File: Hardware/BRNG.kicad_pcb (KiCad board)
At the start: 2 copper layers, 120 x 70 mm, 92 parts, among them J2 MOLEX 105017 0001, J3 CONNETTORE FEMMINA 6 PIN 90°, Q1 BC847, Q2 BC847, Q3 MMBTA42, Q4 BC847, Q5 BC847, SW1 DIPTRONICS NDI-02H-V, U1 LM555N, U2 ATMEGA328-AU, U3 LM555N, U4 CH340G, Y1 16MHz LF XTAL003237, Y2 12MHz LF XTAL003210

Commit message: Fixes #5
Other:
- board text added: "Rev 1 - May 2018 valerionappi.it github.com/5N44P"
- board text removed: "Rev 0 - Mar 2018 valerionappi.it github.com/5N44P"
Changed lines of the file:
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@@
-(kicad_pcb (version 20170123) (host pcbnew "(2017-07-16 revision e797af331)-makepkg")
+(kicad_pcb (version 4) (host pcbnew 4.0.7)
   (general
+    (links 167)
+    (no_connects 1)
+    (area 72.943571 51.449999 211.642858 121.550001)
     (thickness 1.6)
     (drawings 44)
@@
     (visible_elements 7FFFFFFF)
     (pcbplotparams
-      (layerselection 0x010f0_ffffffff)
-      (usegerberextensions false)
+      (layerselection 0x010f0_80000001)
+      (usegerberextensions true)
       (excludeedgelayer true)
       (linewidth 0.100000)
@@
       (hpglpenspeed 20)
       (hpglpendiameter 15)
+      (hpglpenoverlay 2)
       (psnegative false)
       (psa4output false)
@@
       (drillshape 0)
       (scaleselection 1)
-      (outputdirectory illustration/))
+      (outputdirectory /home/valerio/Scrivania/Gerber/))
   )
   (net 0 "")
@@
     (tags "resistor 0805")
     (attr smd)
-    (fp_text reference R4 (at 3.073094 0.118122) (layer F.SilkS)
+    (fp_text reference R4 (at 3.073094 0.118122 360) (layer F.SilkS)
       (effects (font (size 1 1) (thickness 0.15)))
     )
@@
       (effects (font (size 1 1) (thickness 0.15)))
     )
-    (fp_text user %R (at 0 0) (layer F.Fab)
+    (fp_text user %R (at 0 0 360) (layer F.Fab)
       (effects (font (size 1 1) (thickness 0.15)))
     )
@@
   (module customfootprints:0802_side_led (layer F.Cu)
     (at 94.5 105.75 315)
-    (fp_text reference D9 (at 3.535534 -1.414214) (layer F.SilkS)
+    (fp_text reference D9 (at 3.535534 -1.414214 360) (layer F.SilkS)
       (effects (font (size 1 1) (thickness 0.15)))
     )
@@
   (module customfootprints:0802_side_led (layer F.Cu)
     (at 194.952082 65.202082 135)
-    (fp_text reference D10 (at -2.896193 1.767767) (layer F.SilkS)
+    (fp_text reference D10 (at -2.896193 1.767767 360) (layer F.SilkS)
       (effects (font (size 1 1) (thickness 0.15)))
     )
@@
     (effects (font (size 2 2) (thickness 0.4)))
   )
-  (gr_text "Rev 0 - Mar 2018\nvalerionappi.it\ngithub.com/5N44P" (at 138.75 110) (layer F.SilkS)
+  (gr_text "Rev 1 - May 2018\nvalerionappi.it\ngithub.com/5N44P" (at 138.75 110) (layer F.SilkS)
     (effects (font (size 1 1) (thickness 0.2)) (justify left))
   )
@@
     (effects (font (size 1.5 1.5) (thickness 0.3)))
   )
-  (gr_text RX (at 119 103.5) (layer F.SilkS)
+  (gr_text RX (at 118.872 100.33) (layer F.SilkS)
     (effects (font (size 1.5 1.5) (thickness 0.3)))
   )
-  (gr_text TX (at 119 100.5) (layer F.SilkS)
+  (gr_text TX (at 118.872 103.505) (layer F.SilkS)
     (effects (font (size 1.5 1.5) (thickness 0.3)))
   )
@@
   (segment (start 127.75 67.6) (end 127.75 69.25) (width 0.5) (layer F.Cu) (net 3))
   (via (at 127.75 69.25) (size 0.8) (drill 0.4) (layers F.Cu B.Cu) (net 3))
-  (segment (start 101.7 98.64) (end 100.55 98.64) (width 0.5) (layer F.Cu) (net 4))
-  (segment (start 100.55 98.64) (end 100.16 98.25) (width 0.5) (layer F.Cu) (net 4))
-  (segment (start 101.7 98.64) (end 101.11 98.64) (width 0.5) (layer F.Cu) (net 4))
-  (segment (start 134.295028 79) (end 134 79) (width 0.5) (layer F.Cu) (net 6))
-  (segment (start 134.868122 78.426906) (end 134.295028 79) (width 0.5) (layer F.Cu) (net 6))
-  (segment (start 127.25 79) (end 133.434315 79) (width 0.5) (layer B.Cu) (net 6))
-  (segment (start 125.75 80.5) (end 127.25 79) (width 0.5) (layer B.Cu) (net 6))
-  (segment (start 134.868122 77.176906) (end 134.868122 78.426906) (width 0.5) (layer F.Cu) (net 6))
-  (segment (start 133.434315 79) (end 134 79) (width 0.5) (layer B.Cu) (net 6))
-  (via (at 134 79) (size 0.8) (drill 0.4) (layers F.Cu B.Cu) (net 6))
-  (segment (start 125.5 80.75) (end 125.75 80.5) (width 0.5) (layer F.Cu) (net 6))
-  (segment (start 106.25 80.75) (end 125.5 80.75) (width 0.5) (layer F.Cu) (net 6))
-  (via (at 125.75 80.5) (size 0.8) (drill 0.4) (layers F.Cu B.Cu) (net 6))
-  (segment (start 105.850001 81.149999) (end 106.25 80.75) (width 0.5) (layer B.Cu) (net 6))
-  (segment (start 100.5 86.5) (end 105.850001 81.149999) (width 0.5) (layer B.Cu) (net 6))
-  (segment (start 99 86.5) (end 100.5 86.5) (width 0.5) (layer B.Cu) (net 6))
-  (via (at 106.25 80.75) (size 0.8) (drill 0.4) (layers F.Cu B.Cu) (net 6))
   (segment (start 136.718122 71.926906) (end 135.573094 71.926906) (width 0.5) (layer F.Cu) (net 3))
   (segment (start 135.573094 71.926906) (end 135.5 72) (width 0.5) (layer F.Cu) (net 3))
@@
   (segment (start 196.5 105.35) (end 196.5 107) (width 0.5) (layer F.Cu) (net 3))
   (via (at 196.5 107) (size 0.8) (drill 0.4) (layers F.Cu B.Cu) (net 3))
+  (segment (start 101.7 98.64) (end 100.55 98.64) (width 0.5) (layer F.Cu) (net 4))
+  (segment (start 100.55 98.64) (end 100.16 98.25) (width 0.5) (layer F.Cu) (net 4))
+  (segment (start 101.7 98.64) (end 101.11 98.64) (width 0.5) (layer F.Cu) (net 4))
   (segment (start 119.8 64.8) (end 119.8 61.2) (width 0.5) (layer B.Cu) (net 4))
   (via (at 119.8 61.2) (size 0.8) (drill 0.4) (layers F.Cu B.Cu) (net 4))
@@
   (segment (start 157.25 77.5) (end 154.795 77.5) (width 0.5) (layer F.Cu) (net 5))
   (segment (start 154.795 77.5) (end 154.7 77.405) (width 0.5) (layer F.Cu) (net 5))
+  (segment (start 134.295028 79) (end 134 79) (width 0.5) (layer F.Cu) (net 6))
+  (segment (start 134.868122 78.426906) (end 134.295028 79) (width 0.5) (layer F.Cu) (net 6))
+  (segment (start 127.25 79) (end 133.434315 79) (width 0.5) (layer B.Cu) (net 6))
+  (segment (start 125.75 80.5) (end 127.25 79) (width 0.5) (layer B.Cu) (net 6))
+  (segment (start 134.868122 77.176906) (end 134.868122 78.426906) (width 0.5) (layer F.Cu) (net 6))
+  (segment (start 133.434315 79) (end 134 79) (width 0.5) (layer B.Cu) (net 6))
+  (via (at 134 79) (size 0.8) (drill 0.4) (layers F.Cu B.Cu) (net 6))
+  (segment (start 125.5 80.75) (end 125.75 80.5) (width 0.5) (layer F.Cu) (net 6))
+  (segment (start 106.25 80.75) (end 125.5 80.75) (width 0.5) (layer F.Cu) (net 6))
+  (via (at 125.75 80.5) (size 0.8) (drill 0.4) (layers F.Cu B.Cu) (net 6))
+  (segment (start 105.850001 81.149999) (end 106.25 80.75) (width 0.5) (layer B.Cu) (net 6))
+  (segment (start 100.5 86.5) (end 105.850001 81.149999) (width 0.5) (layer B.Cu) (net 6))
+  (segment (start 99 86.5) (end 100.5 86.5) (width 0.5) (layer B.Cu) (net 6))
+  (via (at 106.25 80.75) (size 0.8) (drill 0.4) (layers F.Cu B.Cu) (net 6))
   (segment (start 137.368122 77.276906) (end 139.868122 77.276906) (width 0.5) (layer F.Cu) (net 6))
   (segment (start 134.868122 77.176906) (end 137.268122 77.176906) (width 0.5) (layer F.Cu) (net 6))
@@
     )
     (polygon
-      (pts
-        (xy 94.25 93.25) (xy 94.25 98.5) (xy 97.75 98.5) (xy 97.75 93.25)
+      (pts        (xy 94.25 93.25) (xy 94.25 98.5) (xy 97.75 98.5) (xy 97.75 93.25)
       )
     )

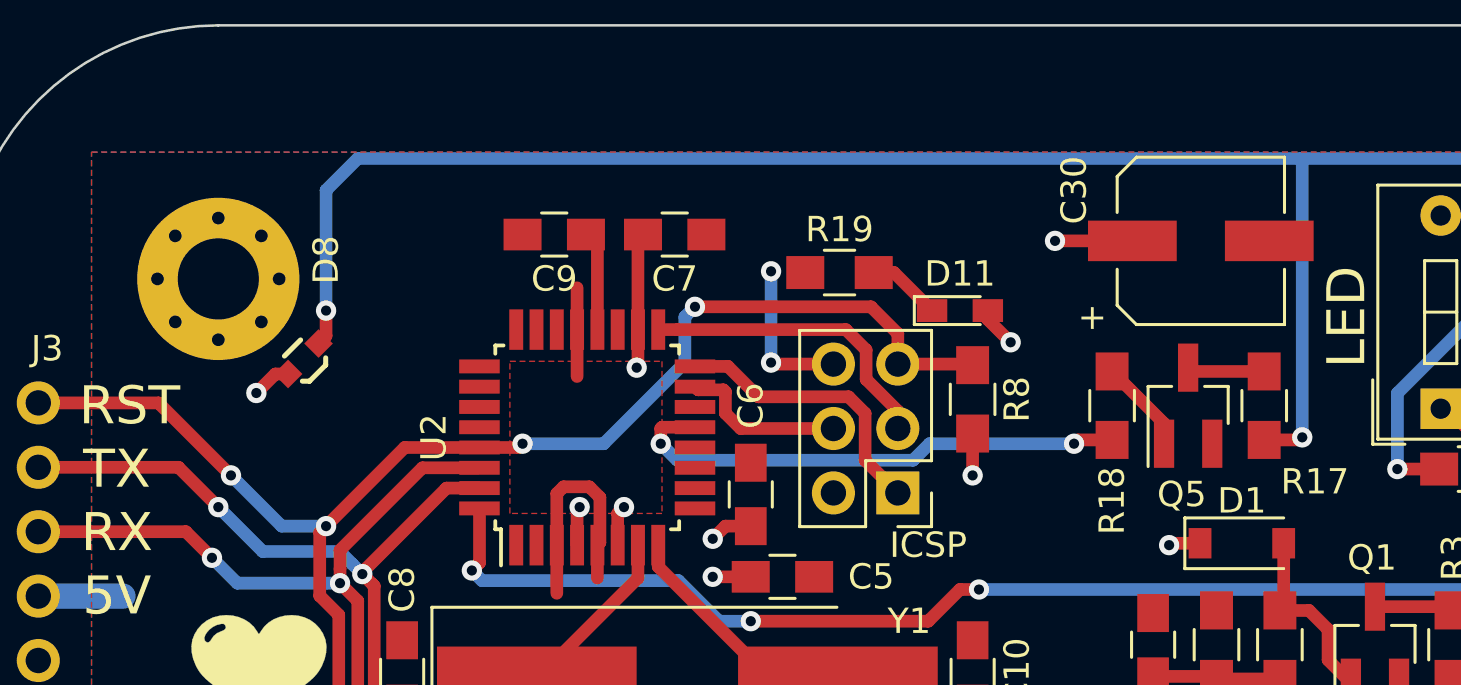
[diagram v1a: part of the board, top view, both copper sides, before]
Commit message: Fixes #4
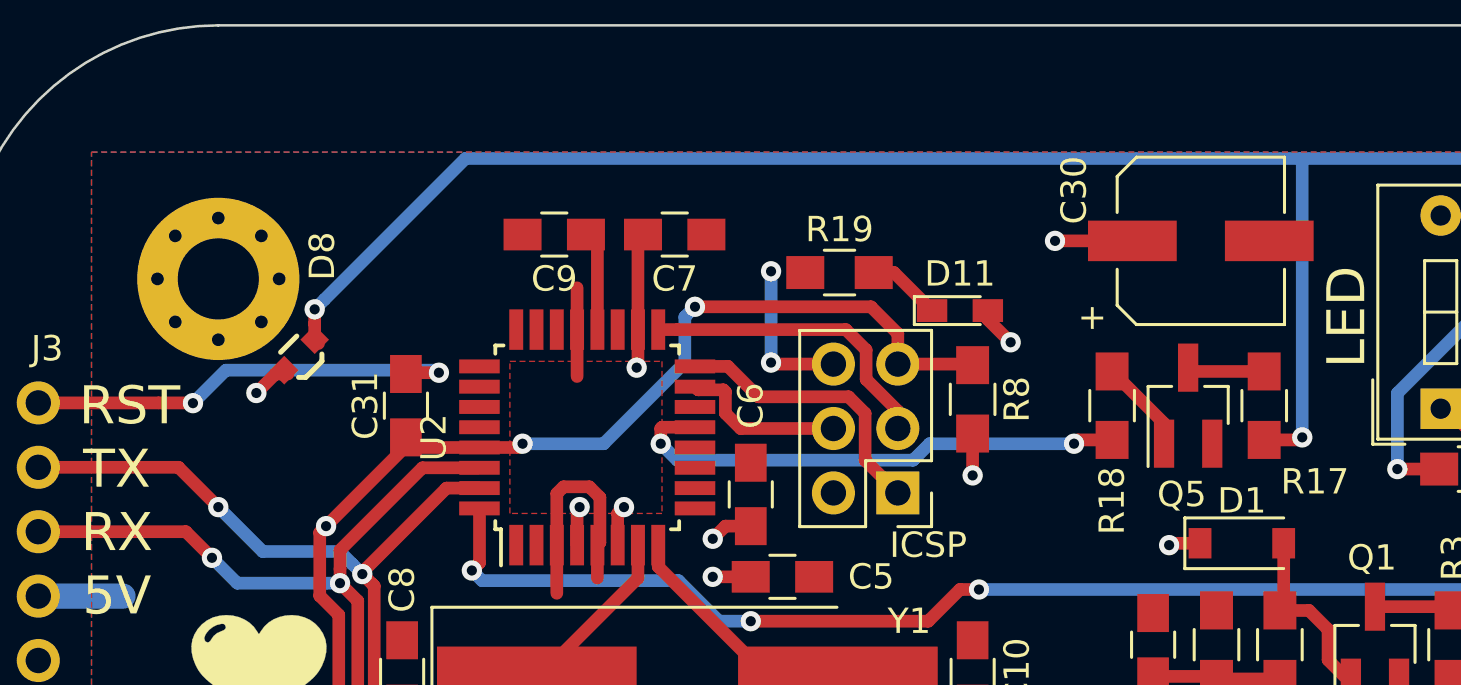
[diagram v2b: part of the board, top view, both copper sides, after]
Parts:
- added C31: 100n, Capacitors_SMD:C_0805_HandSoldering, F.Cu at (105.4, 66.5)
- C3: value 100n -> 22p
- J3: value CONNETTORE FEMMINA 6 PIN 90° -> CONNETTORE 6 PIN 90°
- L1: value 15mH COIL0608-10 -> 15mH
- R1: value 10M YAGEO RC1206JR-0710ML -> 10M
- U2: value ATMEGA328-AU -> ATMEGA328P-AU
- moved D8 0.21 mm to (101.8, 63.9)
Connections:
- J2 pad 4: Net-(J2-Pad4) -> (no net)
- J3 pad 2: Net-(J3-Pad2) -> (no net)
- J3 pad 6: RST -> Net-(C31-Pad1)
- U2 pad 1: Net-(U2-Pad1) -> (no net)
- U2 pad 10: Net-(U2-Pad10) -> (no net)
- U2 pad 11: Net-(U2-Pad11) -> (no net)
- U2 pad 12: Net-(U2-Pad12) -> (no net)
- U2 pad 14: Net-(U2-Pad14) -> (no net)
- U2 pad 19: Net-(U2-Pad19) -> (no net)
- U2 pad 2: Net-(U2-Pad2) -> (no net)
- U2 pad 22: Net-(U2-Pad22) -> (no net)
- U2 pad 23: Net-(U2-Pad23) -> (no net)
- U2 pad 24: Net-(U2-Pad24) -> (no net)
- U2 pad 25: Net-(U2-Pad25) -> (no net)
- U2 pad 26: Net-(U2-Pad26) -> (no net)
- U2 pad 27: Net-(U2-Pad27) -> (no net)
- U2 pad 28: Net-(U2-Pad28) -> (no net)
- U2 pad 9: Net-(U2-Pad9) -> (no net)
- U3 pad 5: Net-(U3-Pad5) -> (no net)
- U4 pad 10: Net-(U4-Pad10) -> (no net)
- U4 pad 11: Net-(U4-Pad11) -> (no net)
- U4 pad 12: Net-(U4-Pad12) -> (no net)
- U4 pad 14: Net-(U4-Pad14) -> (no net)
- U4 pad 15: Net-(U4-Pad15) -> (no net)
- U4 pad 9: Net-(U4-Pad9) -> (no net)
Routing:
- net Net-(C31-Pad1): track 0.00 -> 17.7 mm, vias 0 -> 2
- net RST: track 69.0 -> 55.6 mm, vias 4 -> 3
- net Net-(D10-Pad1): track 308.9 -> 306.5 mm
